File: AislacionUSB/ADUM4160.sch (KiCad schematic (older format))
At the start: 12 parts

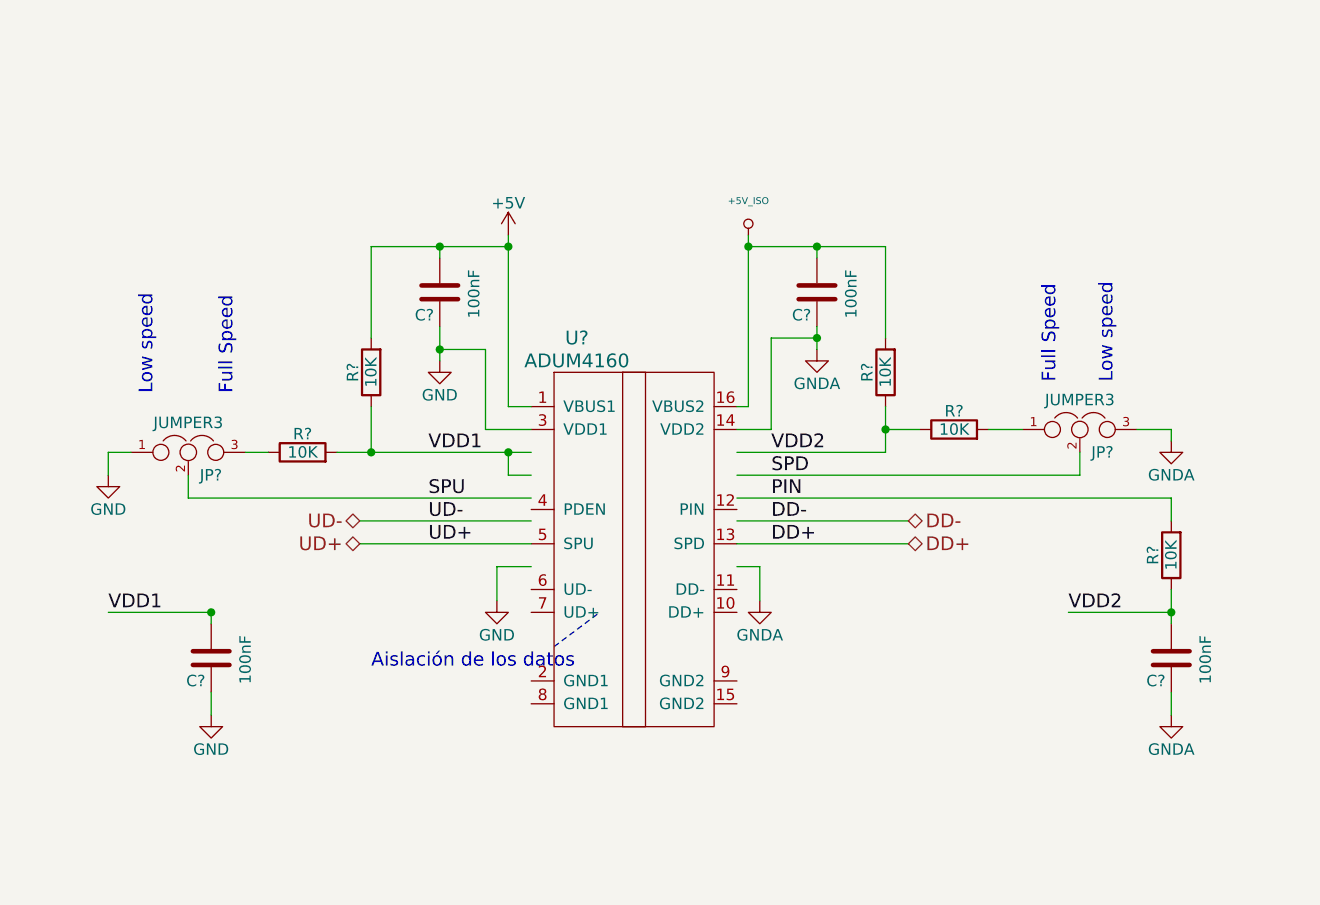
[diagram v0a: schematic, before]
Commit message: Se asociaron los footprints
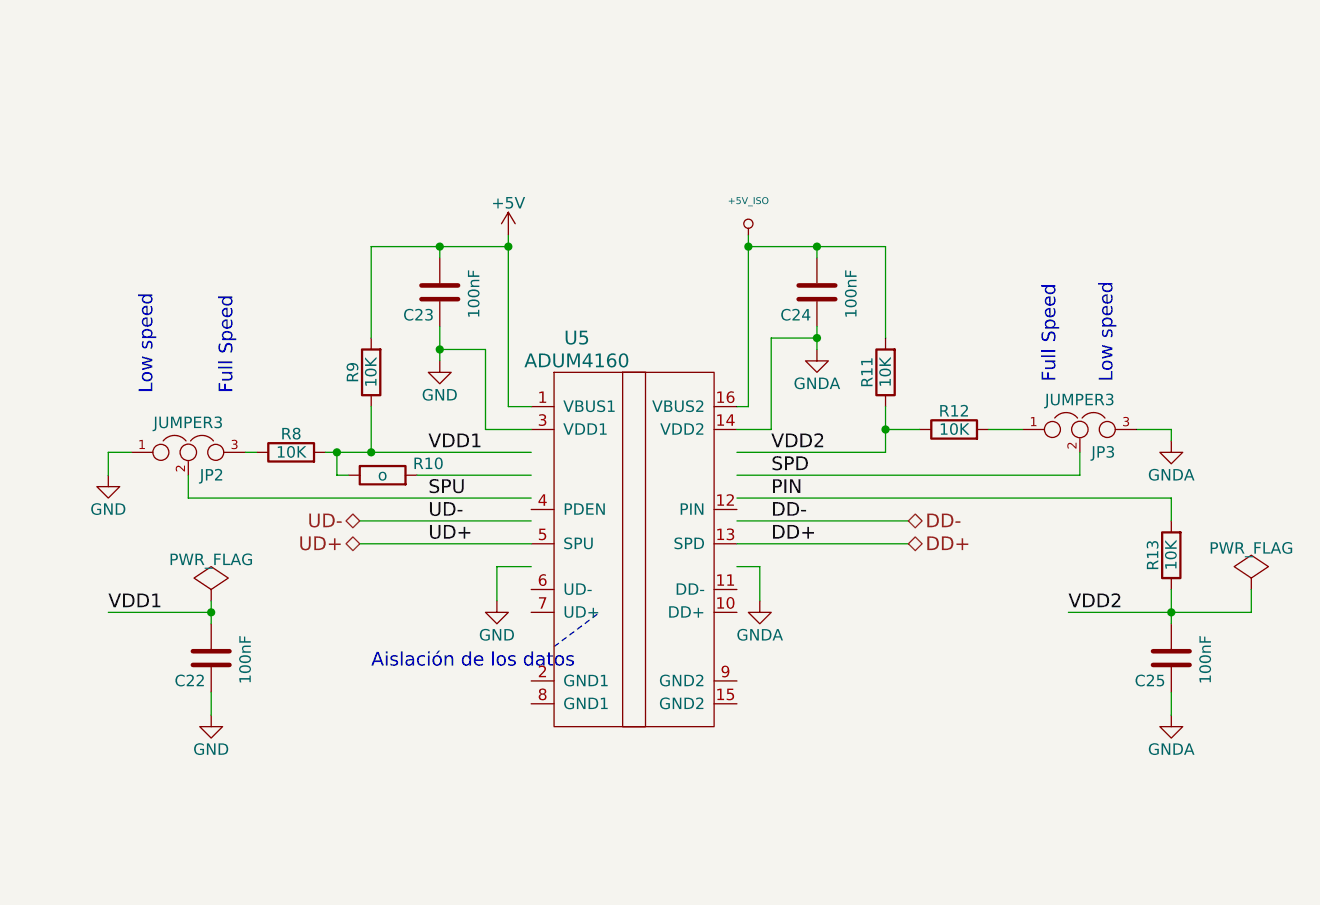
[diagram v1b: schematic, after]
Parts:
- added R10: o, Resistors_SMD:R_0603_HandSoldering, symbol R
- JP2, JP3: renamed from JP?; footprint PIN_ARRAY_3x1 -> Connect:PINHEAD1-3
- U5: renamed from U?; footprint (none) -> Housings_SOIC:SOIC-16_7.5x10.3mm_Pitch1.27mm
- gave numbers to parts that had none: 9
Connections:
- wire segments 51 -> 53
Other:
- moved on the sheet: R8
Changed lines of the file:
@@
 $EndDescr
 $Comp
-L ADUM4160 U?
+L ADUM4160 U5
 U 1 1 578D78CD
 P 5500 3450
-F 0 "U?" H 5250 4150 60  0000 C CNN
+F 0 "U5" H 5250 4150 60  0000 C CNN
 F 1 "ADUM4160" H 5250 4050 60  0000 C CNN
-F 2 "" H 5550 3100 60  0000 C CNN
+F 2 "Housings_SOIC:SOIC-16_7.5x10.3mm_Pitch1.27mm" H 5550 3100 60  0001 C CNN
 F 3 "~" H 5550 3100 60  0000 C CNN
 F 4 "ADUM4160BRWZ-RLTR-ND" H 5500 3450 60  0001 C CNN "Digikey#"
@@
 $EndComp
 $Comp
-L GND #PWR?
+L GND #PWR061
 U 1 1 578D78D4
 P 4900 3900
-F 0 "#PWR?" H 4900 3650 50  0001 C CNN
+F 0 "#PWR061" H 4900 3650 50  0001 C CNN
 F 1 "GND" H 4900 3750 50  0000 C CNN
 F 2 "" H 4900 3900 50  0000 C CNN
@@
 $EndComp
 $Comp
-L GNDA #PWR?
+L GNDA #PWR062
 U 1 1 578D78DA
 P 6050 3900
-F 0 "#PWR?" H 6050 3650 50  0001 C CNN
+F 0 "#PWR062" H 6050 3650 50  0001 C CNN
 F 1 "GNDA" H 6050 3750 50  0000 C CNN
 F 2 "" H 6050 3900 50  0000 C CNN
@@
 $EndComp
 $Comp
-L GNDA #PWR?
+L GNDA #PWR063
 U 1 1 578D78E0
 P 6300 2800
-F 0 "#PWR?" H 6300 2550 50  0001 C CNN
+F 0 "#PWR063" H 6300 2550 50  0001 C CNN
 F 1 "GNDA" H 6300 2650 50  0000 C CNN
 F 2 "" H 6300 2800 50  0000 C CNN
@@
 $EndComp
 $Comp
-L GNDA #PWR?
+L GNDA #PWR064
 U 1 1 578D78F6
 P 7850 4400
-F 0 "#PWR?" H 7850 4150 50  0001 C CNN
+F 0 "#PWR064" H 7850 4150 50  0001 C CNN
 F 1 "GNDA" H 7850 4250 50  0000 C CNN
 F 2 "" H 7850 4400 50  0000 C CNN
@@
 VDD2
 $Comp
-L +5V_ISO #PWR?
+L +5V_ISO #PWR065
 U 1 1 578D78FE
 P 6000 2300
-F 0 "#PWR?" H 6000 2390 20  0001 C CNN
+F 0 "#PWR065" H 6000 2390 20  0001 C CNN
 F 1 "+5V_ISO" H 6000 2450 30  0000 C CNN
 F 2 "" H 6000 2300 60  0000 C CNN
@@
 $EndComp
 $Comp
-L GND #PWR?
+L GND #PWR066
 U 1 1 578D7904
 P 4650 2850
-F 0 "#PWR?" H 4650 2600 50  0001 C CNN
+F 0 "#PWR066" H 4650 2600 50  0001 C CNN
 F 1 "GND" H 4650 2700 50  0000 C CNN
 F 2 "" H 4650 2850 50  0000 C CNN
@@
 SPD
 $Comp
-L R R?
+L R R9
 U 1 1 578D7926
 P 4350 2900
-F 0 "R?" V 4430 2900 50  0000 C CNN
+F 0 "R9" V 4430 2900 50  0000 C CNN
 F 1 "10K" V 4350 2900 50  0000 C CNN
 F 2 "Resistors_SMD:R_0603_HandSoldering" V 4280 2900 50  0001 C CNN
@@
 $EndComp
 $Comp
-L GNDA #PWR?
+L GNDA #PWR067
 U 1 1 578D792D
 P 7850 3200
-F 0 "#PWR?" H 7850 2950 50  0001 C CNN
+F 0 "#PWR067" H 7850 2950 50  0001 C CNN
 F 1 "GNDA" H 7850 3050 50  0000 C CNN
 F 2 "" H 7850 3200 50  0000 C CNN
@@
 $EndComp
 $Comp
-L GND #PWR?
+L GND #PWR068
 U 1 1 578D7933
 P 3200 3350
-F 0 "#PWR?" H 3200 3100 50  0001 C CNN
+F 0 "#PWR068" H 3200 3100 50  0001 C CNN
 F 1 "GND" H 3200 3200 50  0000 C CNN
 F 2 "" H 3200 3350 50  0000 C CNN
@@
 	6000 3050 5950 3050
 Wire Wire Line
-	4200 3250 5050 3250
-Wire Wire Line
-	4950 3350 4950 3250
-Connection ~ 4950 3250
-Wire Wire Line
-	4950 3350 5050 3350
+	4150 3250 5050 3250
+Wire Wire Line
+	4550 3350 5050 3350
 Wire Wire Line
 	3550 3450 5050 3450
@@
 	5150 4100 5350 3950
 $Comp
-L C C?
+L C C23
 U 1 1 578D79AF
 P 4650 2550
-F 0 "C?" H 4675 2650 50  0000 L CNN
+F 0 "C23" H 4675 2650 50  0000 L CNN
 F 1 "100nF" V 4500 2450 50  0000 L CNN
 F 2 "Capacitors_SMD:C_0603_HandSoldering" H 4688 2400 50  0001 C CNN
@@
 $EndComp
 $Comp
-L C C?
+L C C24
 U 1 1 578D79BA
 P 6300 2550
-F 0 "C?" H 6325 2650 50  0000 L CNN
+F 0 "C24" H 6325 2650 50  0000 L CNN
 F 1 "100nF" V 6150 2450 50  0000 L CNN
 F 2 "Capacitors_SMD:C_0603_HandSoldering" H 6338 2400 50  0001 C CNN
@@
 $EndComp
 $Comp
-L +5V #PWR?
+L +5V #PWR069
 U 1 1 578D79D7
 P 4950 2300
-F 0 "#PWR?" H 4950 2150 50  0001 C CNN
+F 0 "#PWR069" H 4950 2150 50  0001 C CNN
 F 1 "+5V" H 4950 2440 50  0000 C CNN
 F 2 "" H 4950 2300 50  0000 C CNN
@@
 	3200 3250 3200 3350
 Wire Wire Line
-	3800 3250 3900 3250
-Wire Wire Line
 	4650 2400 4650 2350
 Connection ~ 4650 2350
@@
 Connection ~ 4650 2800
 $Comp
-L GND #PWR?
+L GND #PWR070
 U 1 1 578E4D04
 P 3650 4400
-F 0 "#PWR?" H 3650 4150 50  0001 C CNN
+F 0 "#PWR070" H 3650 4150 50  0001 C CNN
 F 1 "GND" H 3650 4250 50  0000 C CNN
 F 2 "" H 3650 4400 50  0000 C CNN
@@
 $EndComp
 $Comp
-L C C?
+L C C22
 U 1 1 578E4D4A
 P 3650 4150
-F 0 "C?" H 3675 4250 50  0000 L CNN
+F 0 "C22" H 3675 4250 50  0000 L CNN
 F 1 "100nF" V 3500 4050 50  0000 L CNN
 F 2 "Capacitors_SMD:C_0603_HandSoldering" H 3688 4000 50  0001 C CNN
@@
 VDD1
 Wire Wire Line
-	3650 3950 3650 4000
+	3650 3900 3650 4000
 Wire Wire Line
 	3650 4300 3650 4400
@@
 	3650 3950 3200 3950
 $Comp
-L C C?
+L C C25
 U 1 1 578E51D1
 P 7850 4150
-F 0 "C?" H 7875 4250 50  0000 L CNN
+F 0 "C25" H 7875 4250 50  0000 L CNN
 F 1 "100nF" V 7700 4050 50  0000 L CNN
 F 2 "Capacitors_SMD:C_0603_HandSoldering" H 7888 4000 50  0001 C CNN
@@
 Connection ~ 7850 3950
 Wire Wire Line
-	7850 3950 7400 3950
+	7400 3950 8200 3950
 Wire Wire Line
 	7450 3350 7450 3250
@@
 Connection ~ 6300 2750
 $Comp
-L JUMPER3 JP?
+L JUMPER3 JP2
 U 1 1 578F22B5
 P 3550 3250
-F 0 "JP?" H 3600 3150 50  0000 L CNN
+F 0 "JP2" H 3600 3150 50  0000 L CNN
 F 1 "JUMPER3" H 3550 3350 50  0000 C BNN
-F 2 "PIN_ARRAY_3x1" H 3550 3250 50  0001 C CNN
+F 2 "Connect:PINHEAD1-3" H 3550 3250 50  0001 C CNN
 F 3 "~" H 3550 3250 50  0000 C CNN
 F 4 "Z5375-ND" H 3550 3250 60  0001 C CNN "Digikey#"
@@
 $EndComp
 $Comp
-L JUMPER3 JP?
+L JUMPER3 JP3
 U 1 1 578F23EC
 P 7450 3150
-F 0 "JP?" H 7500 3050 50  0000 L CNN
+F 0 "JP3" H 7500 3050 50  0000 L CNN
 F 1 "JUMPER3" H 7450 3250 50  0000 C BNN
-F 2 "PIN_ARRAY_3x1" H 7450 3150 50  0001 C CNN
+F 2 "Connect:PINHEAD1-3" H 7450 3150 50  0001 C CNN
 F 3 "~" H 7450 3150 50  0000 C CNN
 F 4 "Z5375-ND" H 7450 3150 60  0001 C CNN "Digikey#"
@@
 $EndComp
 $Comp
-L R R?
+L R R12
 U 1 1 578F89A1
 P 6900 3150
-F 0 "R?" V 6980 3150 50  0000 C CNN
+F 0 "R12" V 6980 3150 50  0000 C CNN
 F 1 "10K" V 6900 3150 50  0000 C CNN
 F 2 "Resistors_SMD:R_0603_HandSoldering" V 6830 3150 50  0001 C CNN
@@
 $EndComp
 $Comp
-L R R?
+L R R8
 U 1 1 578F8A0A
-P 4050 3250
-F 0 "R?" V 4130 3250 50  0000 C CNN
-F 1 "10K" V 4050 3250 50  0000 C CNN
-F 2 "Resistors_SMD:R_0603_HandSoldering" V 3980 3250 50  0001 C CNN
-F 3 "" H 4050 3250 50  0000 C CNN
-F 4 "RES SMD 10K OHM 5% 1/10W 0603" V 4050 3250 60  0001 C CNN "Desc"
-F 5 "P10KGTR-ND" V 4050 3250 60  0001 C CNN "Digikey#"
-F 6 "ERJ-3GEYJ103V" V 4050 3250 60  0001 C CNN "Manf#"
-F 7 "Panasonic Electronic Components" V 4050 3250 60  0001 C CNN "Manf"
-	1    4050 3250
+P 4000 3250
+F 0 "R8" V 4080 3250 50  0000 C CNN
+F 1 "10K" V 4000 3250 50  0000 C CNN
+F 2 "Resistors_SMD:R_0603_HandSoldering" V 3930 3250 50  0001 C CNN
+F 3 "" H 4000 3250 50  0000 C CNN
+F 4 "RES SMD 10K OHM 5% 1/10W 0603" V 4000 3250 60  0001 C CNN "Desc"
+F 5 "P10KGTR-ND" V 4000 3250 60  0001 C CNN "Digikey#"
+F 6 "ERJ-3GEYJ103V" V 4000 3250 60  0001 C CNN "Manf#"
+F 7 "Panasonic Electronic Components" V 4000 3250 60  0001 C CNN "Manf"
+	1    4000 3250
 	0    -1   -1   0
 $EndComp
 $Comp
-L R R?
+L R R13
 U 1 1 578F8DC6
 P 7850 3700
-F 0 "R?" V 7930 3700 50  0000 C CNN
+F 0 "R13" V 7930 3700 50  0000 C CNN
 F 1 "10K" V 7850 3700 50  0000 C CNN
 F 2 "Resistors_SMD:R_0603_HandSoldering" V 7780 3700 50  0001 C CNN
@@
 $EndComp
 $Comp
-L R R?
+L R R11
 U 1 1 578F8E33
 P 6600 2900
-F 0 "R?" V 6680 2900 50  0000 C CNN
+F 0 "R11" V 6680 2900 50  0000 C CNN
 F 1 "10K" V 6600 2900 50  0000 C CNN
 F 2 "Resistors_SMD:R_0603_HandSoldering" V 6530 2900 50  0001 C CNN
@@
 	-1   0    0    1
 $EndComp
+$Comp
+L PWR_FLAG #FLG071
+U 1 1 57905994
+P 3650 3900
+F 0 "#FLG071" H 3650 3995 50  0001 C CNN
+F 1 "PWR_FLAG" H 3650 4080 50  0000 C CNN
+F 2 "" H 3650 3900 50  0000 C CNN
+F 3 "" H 3650 3900 50  0000 C CNN
+	1    3650 3900
+	1    0    0    -1
+$EndComp
+$Comp
+L PWR_FLAG #FLG072
+U 1 1 579059F8
+P 8200 3850
+F 0 "#FLG072" H 8200 3945 50  0001 C CNN
+F 1 "PWR_FLAG" H 8200 4030 50  0000 C CNN
+F 2 "" H 8200 3850 50  0000 C CNN
+F 3 "" H 8200 3850 50  0000 C CNN
+	1    8200 3850
+	1    0    0    -1
+$EndComp
+Wire Wire Line
+	8200 3950 8200 3850
+$Comp
+L R R10
+U 1 1 5790E825
+P 4400 3350
+F 0 "R10" V 4450 3150 50  0000 C CNN
+F 1 "o" V 4400 3350 50  0000 C CNN
+F 2 "Resistors_SMD:R_0603_HandSoldering" V 4330 3350 50  0001 C CNN
+F 3 "" H 4400 3350 50  0000 C CNN
+F 4 "RES SMD 0.0OHM JUMPER 1/10W 0603" V 4400 3350 60  0001 C CNN "Desc"
+F 5 "P0.0GTR-ND" V 4400 3350 60  0001 C CNN "Digikey#"
+F 6 "ERJ-3GEY0R00V" V 4400 3350 60  0001 C CNN "Manf#"
+F 7 "Panasonic Electronic Components" V 4400 3350 60  0001 C CNN "Manf"
+	1    4400 3350
+	0    -1   -1   0
+$EndComp
+Wire Wire Line
+	4250 3350 4200 3350
+Wire Wire Line
+	4200 3350 4200 3250
+Connection ~ 4200 3250
+Wire Wire Line
+	3850 3250 3800 3250
 $EndSCHEMATC

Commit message: Rev01 – Se incorporaron las observaciones realizadas en la primera revisión del esquemático - doc:
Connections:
- net labels removed: PIN, SPD, SPU, VDD1, VDD2
- wire segments 53 -> 52
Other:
- note added: "R8, R9, R11, R12, R13 \npueden omitirse utilizando \nresistencias de 0 Ohms."
- moved on the sheet: C22, C23, C24, JP2, JP3, R10, R12, R8, R9, U5

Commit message: Se agregaron cambios sugeridos por el docente - DOC:Sugerencias Docente 20160724
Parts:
- C22, C23, C24, C25: footprint Capacitors_SMD:C_0603_HandSoldering -> AislacionUSB:C_0603_HandSoldering
- JP2, JP3: footprint Connect:PINHEAD1-3 -> AislacionUSB:PIN_ARRAY_3x1
- R10, R11, R12, R13, R8, R9: footprint Resistors_SMD:R_0603_HandSoldering -> AislacionUSB:R_0603_HandSoldering
- U5: footprint Housings_SOIC:SOIC-16_7.5x10.3mm_Pitch1.27mm -> AislacionUSB:ADUM4160
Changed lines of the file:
@@
 EESchema Schematic File Version 2
-LIBS:USBCableIsolatorCircuit-rescue
 LIBS:power
 LIBS:device
@@
 LIBS:valves
 LIBS:USBCableIsolatorCircuit
-LIBS:CIAA_K60
 LIBS:USBCableIsolatorCircuit-cache
 EELAYER 25 0
@@
 encoding utf-8
 Sheet 2 2
-Title "Aislacion de USB - ADUM4160"
+Title "Aislador USB para uso industrial."
 Date ""
 Rev "01"
@@
 $EndDescr
 $Comp
-L GND #PWR056
+L GND #PWR061
 U 1 1 578D78D4
 P 4900 4100
-F 0 "#PWR056" H 4900 3850 50  0001 C CNN
+F 0 "#PWR061" H 4900 3850 50  0001 C CNN
 F 1 "GND" H 4900 3950 50  0000 C CNN
 F 2 "" H 4900 4100 50  0000 C CNN
@@
 $EndComp
 $Comp
-L GNDA #PWR057
+L GNDA #PWR062
 U 1 1 578D78DA
 P 6050 4100
-F 0 "#PWR057" H 6050 3850 50  0001 C CNN
+F 0 "#PWR062" H 6050 3850 50  0001 C CNN
 F 1 "GNDA" H 6050 3950 50  0000 C CNN
 F 2 "" H 6050 4100 50  0000 C CNN
@@
 $EndComp
 $Comp
-L GNDA #PWR058
+L GNDA #PWR063
 U 1 1 578D78E0
 P 5750 2200
-F 0 "#PWR058" H 5750 1950 50  0001 C CNN
+F 0 "#PWR063" H 5750 1950 50  0001 C CNN
 F 1 "GNDA" H 5750 2050 50  0000 C CNN
 F 2 "" H 5750 2200 50  0000 C CNN
@@
 $EndComp
 $Comp
-L +5V_ISO #PWR059
+L +5V_ISO #PWR064
 U 1 1 578D78FE
 P 6050 1650
-F 0 "#PWR059" H 6050 1740 20  0001 C CNN
+F 0 "#PWR064" H 6050 1740 20  0001 C CNN
 F 1 "+5V_ISO" H 6050 1800 30  0000 C CNN
 F 2 "" H 6050 1650 60  0000 C CNN
@@
 $EndComp
 $Comp
-L GND #PWR060
+L GND #PWR065
 U 1 1 578D7904
 P 5250 2200
-F 0 "#PWR060" H 5250 1950 50  0001 C CNN
+F 0 "#PWR065" H 5250 1950 50  0001 C CNN
 F 1 "GND" H 5250 2050 50  0000 C CNN
 F 2 "" H 5250 2200 50  0000 C CNN
@@
 F 0 "R9" V 4930 2650 50  0000 C CNN
 F 1 "10K" V 4850 2650 50  0000 C CNN
-F 2 "Resistors_SMD:R_0603_HandSoldering" V 4780 2650 50  0001 C CNN
+F 2 "AislacionUSB:R_0603_HandSoldering" V 4780 2650 50  0001 C CNN
 F 3 "" H 4850 2650 50  0000 C CNN
 F 4 "RES SMD 10K OHM 5% 1/10W 0603" V 4850 2650 60  0001 C CNN "Desc"
@@
 $EndComp
 $Comp
-L GNDA #PWR061
+L GNDA #PWR066
 U 1 1 578D792D
 P 7850 2500
-F 0 "#PWR061" H 7850 2250 50  0001 C CNN
+F 0 "#PWR066" H 7850 2250 50  0001 C CNN
 F 1 "GNDA" H 7850 2350 50  0000 C CNN
 F 2 "" H 7850 2500 50  0000 C CNN
@@
 $EndComp
 $Comp
-L GND #PWR062
+L GND #PWR067
 U 1 1 578D7933
 P 2900 2550
-F 0 "#PWR062" H 2900 2300 50  0001 C CNN
+F 0 "#PWR067" H 2900 2300 50  0001 C CNN
 F 1 "GND" H 2900 2400 50  0000 C CNN
 F 2 "" H 2900 2550 50  0000 C CNN
@@
 F 0 "C23" H 5350 1850 50  0000 L CNN
 F 1 "100nF" V 5350 2000 50  0000 L CNN
-F 2 "Capacitors_SMD:C_0603_HandSoldering" H 5288 1800 50  0001 C CNN
+F 2 "AislacionUSB:C_0603_HandSoldering" H 5288 1800 50  0001 C CNN
 F 3 "~" H 5250 1950 50  0000 C CNN
 F 4 "399-1096-1-ND" H 5250 1950 60  0001 C CNN "Digikey#"
@@
 F 0 "C24" H 5550 1800 50  0000 L CNN
 F 1 "100nF" V 5600 1950 50  0000 L CNN
-F 2 "Capacitors_SMD:C_0603_HandSoldering" H 5788 1800 50  0001 C CNN
+F 2 "AislacionUSB:C_0603_HandSoldering" H 5788 1800 50  0001 C CNN
 F 3 "~" H 5750 1950 50  0000 C CNN
 F 4 "399-1096-1-ND" H 5750 1950 60  0001 C CNN "Digikey#"
@@
 $EndComp
 $Comp
-L +5V #PWR063
+L +5V #PWR068
 U 1 1 578D79D7
 P 4950 1650
-F 0 "#PWR063" H 4950 1500 50  0001 C CNN
+F 0 "#PWR068" H 4950 1500 50  0001 C CNN
 F 1 "+5V" H 4950 1790 50  0000 C CNN
 F 2 "" H 4950 1650 50  0000 C CNN
@@
 UD+
 $Comp
-L GND #PWR064
+L GND #PWR069
 U 1 1 578E4D04
 P 3800 2900
-F 0 "#PWR064" H 3800 2650 50  0001 C CNN
+F 0 "#PWR069" H 3800 2650 50  0001 C CNN
 F 1 "GND" H 3800 2750 50  0000 C CNN
 F 2 "" H 3800 2900 50  0000 C CNN
@@
 F 0 "C22" H 4125 2950 50  0000 L CNN
 F 1 "100nF" V 3950 2750 50  0000 L CNN
-F 2 "Capacitors_SMD:C_0603_HandSoldering" H 4138 2700 50  0001 C CNN
+F 2 "AislacionUSB:C_0603_HandSoldering" H 4138 2700 50  0001 C CNN
 F 3 "~" H 4100 2850 50  0000 C CNN
 F 4 "399-1096-1-ND" H 4100 2850 60  0001 C CNN "Digikey#"
@@
 F 0 "JP2" H 3300 2350 50  0000 L CNN
 F 1 "JUMPER3" H 3250 2550 50  0000 C BNN
-F 2 "Connect:PINHEAD1-3" H 3250 2450 50  0001 C CNN
+F 2 "AislacionUSB:PIN_ARRAY_3x1" H 3250 2450 50  0001 C CNN
 F 3 "~" H 3250 2450 50  0000 C CNN
 F 4 "Z5375-ND" H 3250 2450 60  0001 C CNN "Digikey#"
@@
 F 0 "JP3" H 7500 2350 50  0000 L CNN
 F 1 "JUMPER3" H 7450 2550 50  0000 C BNN
-F 2 "Connect:PINHEAD1-3" H 7450 2450 50  0001 C CNN
+F 2 "AislacionUSB:PIN_ARRAY_3x1" H 7450 2450 50  0001 C CNN
 F 3 "~" H 7450 2450 50  0000 C CNN
 F 4 "Z5375-ND" H 7450 2450 60  0001 C CNN "Digikey#"
@@
 F 0 "R12" V 6330 3200 50  0000 C CNN
 F 1 "10K" V 6250 3200 50  0000 C CNN
-F 2 "Resistors_SMD:R_0603_HandSoldering" V 6180 3200 50  0001 C CNN
+F 2 "AislacionUSB:R_0603_HandSoldering" V 6180 3200 50  0001 C CNN
 F 3 "" H 6250 3200 50  0000 C CNN
 F 4 "RES SMD 10K OHM 5% 1/10W 0603" V 6250 3200 60  0001 C CNN "Desc"
@@
 F 0 "R8" V 4480 2650 50  0000 C CNN
 F 1 "10K" V 4400 2650 50  0000 C CNN
-F 2 "Resistors_SMD:R_0603_HandSoldering" V 4330 2650 50  0001 C CNN
+F 2 "AislacionUSB:R_0603_HandSoldering" V 4330 2650 50  0001 C CNN
 F 3 "" H 4400 2650 50  0000 C CNN
 F 4 "RES SMD 10K OHM 5% 1/10W 0603" V 4400 2650 60  0001 C CNN "Desc"
@@
 $EndComp
 $Comp
-L PWR_FLAG #FLG065
+L PWR_FLAG #FLG070
 U 1 1 57905994
 P 4650 2500
-F 0 "#FLG065" H 4650 2595 50  0001 C CNN
+F 0 "#FLG070" H 4650 2595 50  0001 C CNN
 F 1 "PWR_FLAG" H 4650 2680 50  0000 C CNN
 F 2 "" H 4650 2500 50  0000 C CNN
@@
 F 0 "R10" V 4750 3000 50  0000 C CNN
 F 1 "o" V 4700 3200 50  0000 C CNN
-F 2 "Resistors_SMD:R_0603_HandSoldering" V 4630 3200 50  0001 C CNN
+F 2 "AislacionUSB:R_0603_HandSoldering" V 4630 3200 50  0001 C CNN
 F 3 "" H 4700 3200 50  0000 C CNN
 F 4 "RES SMD 0.0OHM JUMPER 1/10W 0603" V 4700 3200 60  0001 C CNN "Desc"
@@
 F 0 "U5" H 5500 3850 60  0000 C CNN
 F 1 "ADUM4160" H 5500 3750 60  0000 C CNN
-F 2 "Housings_SOIC:SOIC-16_7.5x10.3mm_Pitch1.27mm" H 5550 2800 60  0001 C CNN
+F 2 "AislacionUSB:ADUM4160" H 5550 2800 60  0001 C CNN
 F 3 "~" H 5550 2800 60  0000 C CNN
 F 4 "ADUM4160BRWZ-RLTR-ND" H 5500 3150 60  0001 C CNN "Digikey#"
@@
 F 0 "R11" V 6230 2650 50  0000 C CNN
 F 1 "10K" V 6150 2650 50  0000 C CNN
-F 2 "Resistors_SMD:R_0603_HandSoldering" V 6080 2650 50  0001 C CNN
+F 2 "AislacionUSB:R_0603_HandSoldering" V 6080 2650 50  0001 C CNN
 F 3 "" H 6150 2650 50  0000 C CNN
 F 4 "RES SMD 10K OHM 5% 1/10W 0603" V 6150 2650 60  0001 C CNN "Desc"
@@
 $EndComp
 $Comp
-L GNDA #PWR066
+L GNDA #PWR071
 U 1 1 5790657D
 P 7100 2900
-F 0 "#PWR066" H 7100 2650 50  0001 C CNN
+F 0 "#PWR071" H 7100 2650 50  0001 C CNN
 F 1 "GNDA" H 7100 2750 50  0000 C CNN
 F 2 "" H 7100 2900 50  0000 C CNN
@@
 F 0 "C25" H 6925 2950 50  0000 L CNN
 F 1 "100nF" V 6750 2750 50  0000 L CNN
-F 2 "Capacitors_SMD:C_0603_HandSoldering" H 6938 2700 50  0001 C CNN
+F 2 "AislacionUSB:C_0603_HandSoldering" H 6938 2700 50  0001 C CNN
 F 3 "~" H 6900 2850 50  0000 C CNN
 F 4 "399-1096-1-ND" H 6900 2850 60  0001 C CNN "Digikey#"
@@
 F 0 "R13" V 6630 2650 50  0000 C CNN
 F 1 "10K" V 6550 2650 50  0000 C CNN
-F 2 "Resistors_SMD:R_0603_HandSoldering" V 6480 2650 50  0001 C CNN
+F 2 "AislacionUSB:R_0603_HandSoldering" V 6480 2650 50  0001 C CNN
 F 3 "" H 6550 2650 50  0000 C CNN
 F 4 "RES SMD 10K OHM 5% 1/10W 0603" V 6550 2650 60  0001 C CNN "Desc"
@@
 $EndComp
 $Comp
-L PWR_FLAG #FLG067
+L PWR_FLAG #FLG072
 U 1 1 57906A8D
 P 6350 2500
-F 0 "#FLG067" H 6350 2595 50  0001 C CNN
+F 0 "#FLG072" H 6350 2595 50  0001 C CNN
 F 1 "PWR_FLAG" H 6350 2680 50  0000 C CNN
 F 2 "" H 6350 2500 50  0000 C CNN
